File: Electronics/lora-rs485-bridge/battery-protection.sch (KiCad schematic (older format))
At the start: 3 parts

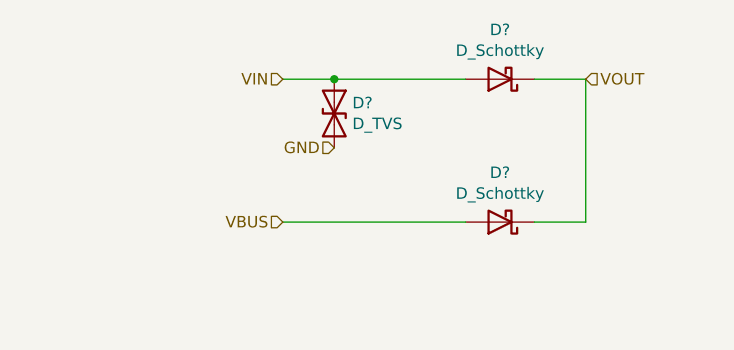
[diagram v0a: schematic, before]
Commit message: Some PCB routing is done
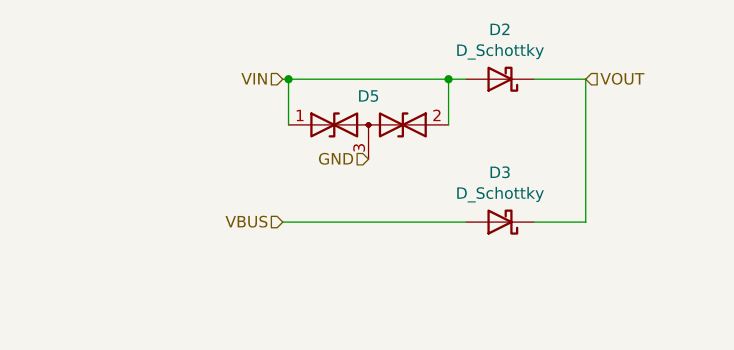
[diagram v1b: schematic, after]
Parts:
- removed D?: D_TVS, symbol Device:D_TVS
- removed D? (x2): D_Schottky, symbol Device:D_Schottky
- added D2, D3: D_Schottky, Diode_SMD:D_SOD-123F, symbol Device:D_Schottky
- added D5: D_TVS_x2_AAC, miceuz-lib:SC89, symbol Device:D_TVS_x2_AAC
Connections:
- net GND: now also D5.3 (common)
- net VBUS: now also D3.2 (A)
- net VIN: now also D2.2 (A), D5.1 (A1), D5.2 (A2)
- net VOUT: now also D2.1 (K), D3.1 (K)
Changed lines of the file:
@@
 EESchema Schematic File Version 5
-LIBS:lora-bridge-cache
 EELAYER 30 0
 EELAYER END
 $Descr A4 11693 8268
 encoding utf-8
-Sheet 2 5
+Sheet 5 5
 Title ""
 Date ""
@@
 	3500 1800 3725 1800
 $Comp
-L Device:D_Schottky D?
+L Device:D_Schottky D2
 U 1 1 5D8754F6
 P 3350 1800
-F 0 "D?" H 3350 1584 50  0000 C CNN
+F 0 "D2" H 3350 1584 50  0000 C CNN
 F 1 "D_Schottky" H 3350 1675 50  0000 C CNN
-F 2 "" H 3350 1800 50  0001 C CNN
+F 2 "Diode_SMD:D_SOD-123F" H 3350 1800 50  0001 C CNN
 F 3 "~" H 3350 1800 50  0001 C CNN
+F 4 "ON SEMICONDUCTOR" H 3350 1800 50  0001 C CNN "Manufacturer"
+F 5 "MBR1020VL" H 3350 1800 50  0001 C CNN "PartNo"
 	1    3350 1800
 	-1   0    0    1
 $EndComp
 $Comp
-L Device:D_TVS D?
-U 1 1 5D877A3B
-P 2625 1950
-F 0 "D?" V 2579 2029 50  0000 L CNN
-F 1 "D_TVS" V 2670 2029 50  0000 L CNN
-F 2 "" H 2625 1950 50  0001 C CNN
-F 3 "~" H 2625 1950 50  0001 C CNN
-	1    2625 1950
-	0    1    1    0
-$EndComp
-Wire Wire Line
-	2400 1800 2625 1800
-Connection ~ 2625 1800
-Wire Wire Line
-	2625 1800 3200 1800
-$Comp
-L Device:D_Schottky D?
-U 1 1 5D8754F6
+L Device:D_Schottky D3
+U 1 1 5D86D14C
 P 3350 2425
-F 0 "D?" H 3350 2209 50  0000 C CNN
+F 0 "D3" H 3350 2209 50  0000 C CNN
 F 1 "D_Schottky" H 3350 2300 50  0000 C CNN
-F 2 "" H 3350 2425 50  0001 C CNN
+F 2 "Diode_SMD:D_SOD-123F" H 3350 2425 50  0001 C CNN
 F 3 "~" H 3350 2425 50  0001 C CNN
+F 4 "ON SEMICONDUCTOR" H 3350 2425 50  0001 C CNN "Manufacturer"
+F 5 "MBR1020VL" H 3350 2425 50  0001 C CNN "PartNo"
 	1    3350 2425
 	-1   0    0    1
@@
 Wire Wire Line
 	2400 2425 3200 2425
-Text HLabel 2625 2100 0    50   Input ~ 0
+Text HLabel 2775 2150 0    50   Input ~ 0
 GND
+$Comp
+L Device:D_TVS_x2_AAC D5
+U 1 1 5D880D1E
+P 2775 2000
+F 0 "D5" H 2775 2125 50  0000 C CNN
+F 1 "D_TVS_x2_AAC" H 2775 2125 50  0001 C CNN
+F 2 "miceuz-lib:SC89" H 2625 2000 50  0001 C CNN
+F 3 "~" H 2625 2000 50  0001 C CNN
+F 4 "ON SEMICONDUCTOR" H 725 300 50  0001 C CNN "Manufacturer"
+F 5 " NZL5V6AXV3T1G" H 725 300 50  0001 C CNN "PartNo"
+	1    2775 2000
+	1    0    0    -1
+$EndComp
+Wire Wire Line
+	2400 1800 2425 1800
+Wire Wire Line
+	2425 2000 2425 1800
+Connection ~ 2425 1800
+Wire Wire Line
+	2425 1800 3125 1800
+Wire Wire Line
+	3125 2000 3125 1800
+Connection ~ 3125 1800
+Wire Wire Line
+	3125 1800 3200 1800
 $EndSCHEMATC

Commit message: Add ESD protection to i2c lines, change VIN TVS diode to higher voltage, add series resistors to SPI lines, compress the PCB to be at width of typical 4xAA battery holder
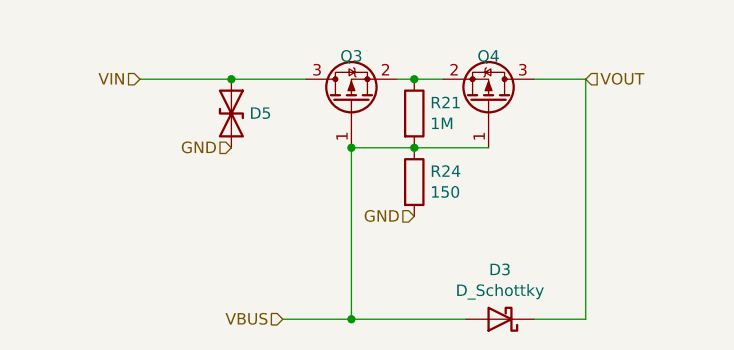
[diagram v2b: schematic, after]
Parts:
- removed D2: D_Schottky, Diode_SMD:D_SOD-123F, symbol Device:D_Schottky
- removed D5: D_TVS_x2_AAC, miceuz-lib:SC89, symbol Device:D_TVS_x2_AAC
- added D5: D_TVS, Diode_SMD:D_SOD-123F, symbol Device:D_TVS
- added Q3, Q4: Q_PMOS_GSD, Package_TO_SOT_SMD:SOT-23, symbol Device:Q_PMOS_GSD
- added R21: 1M, Resistor_SMD:R_0603_1608Metric, symbol Device:R
- added R24: 150, Resistor_SMD:R_0603_1608Metric, symbol Device:R
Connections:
- net GND: now also D5.2 (A2), R24.2
- net VBUS: now also Q3.1 (G), Q4.1 (G), R21.2, R24.1
- net VIN: now also D5.1 (A1), Q3.3 (D)
- net VOUT: now also Q4.3 (D)
- new net: Q3.2 (S), Q4.2 (S), R21.1
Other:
- moved on the sheet: D3
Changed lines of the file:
@@
 $Descr A4 11693 8268
 encoding utf-8
-Sheet 5 5
+Sheet 4 5
 Title ""
 Date ""
@@
 Comment9 ""
 $EndDescr
-Text HLabel 2400 1800 0    50   Input ~ 0
+Text HLabel 1775 1800 0    50   Input ~ 0
 VIN
 Text HLabel 3725 1800 2    50   Input ~ 0
 VOUT
-Text HLabel 2400 2425 0    50   Input ~ 0
+Text HLabel 2400 2850 0    50   Input ~ 0
 VBUS
 Wire Wire Line
 	3500 1800 3725 1800
 $Comp
-L Device:D_Schottky D2
-U 1 1 5D8754F6
-P 3350 1800
-F 0 "D2" H 3350 1584 50  0000 C CNN
-F 1 "D_Schottky" H 3350 1675 50  0000 C CNN
-F 2 "Diode_SMD:D_SOD-123F" H 3350 1800 50  0001 C CNN
-F 3 "~" H 3350 1800 50  0001 C CNN
-F 4 "ON SEMICONDUCTOR" H 3350 1800 50  0001 C CNN "Manufacturer"
-F 5 "MBR1020VL" H 3350 1800 50  0001 C CNN "PartNo"
-	1    3350 1800
-	-1   0    0    1
-$EndComp
-$Comp
 L Device:D_Schottky D3
 U 1 1 5D86D14C
-P 3350 2425
-F 0 "D3" H 3350 2209 50  0000 C CNN
-F 1 "D_Schottky" H 3350 2300 50  0000 C CNN
-F 2 "Diode_SMD:D_SOD-123F" H 3350 2425 50  0001 C CNN
-F 3 "~" H 3350 2425 50  0001 C CNN
-F 4 "ON SEMICONDUCTOR" H 3350 2425 50  0001 C CNN "Manufacturer"
-F 5 "MBR1020VL" H 3350 2425 50  0001 C CNN "PartNo"
-	1    3350 2425
+P 3350 2850
+F 0 "D3" H 3350 2634 50  0000 C CNN
+F 1 "D_Schottky" H 3350 2725 50  0000 C CNN
+F 2 "Diode_SMD:D_SOD-123F" H 3350 2850 50  0001 C CNN
+F 3 "~" H 3350 2850 50  0001 C CNN
+F 4 "ON SEMICONDUCTOR" H 3350 2850 50  0001 C CNN "Manufacturer"
+F 5 "MBR1020VL" H 3350 2850 50  0001 C CNN "PartNo"
+	1    3350 2850
 	-1   0    0    1
 $EndComp
 Wire Wire Line
-	3725 1800 3725 2425
+	3725 1800 3725 2850
 Wire Wire Line
-	3500 2425 3725 2425
+	3500 2850 3725 2850
 Wire Wire Line
-	2400 2425 3200 2425
-Text HLabel 2775 2150 0    50   Input ~ 0
+	2400 2850 2700 2850
+Text HLabel 2175 2100 0    50   Input ~ 0
 GND
 $Comp
-L Device:D_TVS_x2_AAC D5
-U 1 1 5D880D1E
-P 2775 2000
-F 0 "D5" H 2775 2125 50  0000 C CNN
-F 1 "D_TVS_x2_AAC" H 2775 2125 50  0001 C CNN
-F 2 "miceuz-lib:SC89" H 2625 2000 50  0001 C CNN
-F 3 "~" H 2625 2000 50  0001 C CNN
-F 4 "ON SEMICONDUCTOR" H 725 300 50  0001 C CNN "Manufacturer"
-F 5 " NZL5V6AXV3T1G" H 725 300 50  0001 C CNN "PartNo"
-	1    2775 2000
+L Device:D_TVS D5
+U 1 1 5DC183A7
+P 2175 1950
+F 0 "D5" V 2175 2029 50  0000 L CNN
+F 1 "D_TVS" V 2220 2029 50  0001 L CNN
+F 2 "Diode_SMD:D_SOD-123F" H 2175 1950 50  0001 C CNN
+F 3 "~" H 2175 1950 50  0001 C CNN
+F 4 "SMF11A" H 2175 1950 50  0001 C CNN "PartNo"
+F 5 "Littlefuse" H 2175 1950 50  0001 C CNN "Manufacturer"
+	1    2175 1950
+	0    1    1    0
+$EndComp
+Wire Wire Line
+	1775 1800 2175 1800
+$Comp
+L Device:Q_PMOS_GSD Q3
+U 1 1 5DC1ADD3
+P 2700 1900
+F 0 "Q3" V 2900 1900 50  0000 C CNN
+F 1 "Q_PMOS_GSD" V 2937 1900 50  0001 C CNN
+F 2 "Package_TO_SOT_SMD:SOT-23" H 2900 2000 29  0001 C CNN
+F 3 "" H 2700 1900 60  0000 C CNN
+F 4 "NX2301P,215 " H 2700 1900 60  0001 C CNN "PartNo"
+F 5 "NXP" H 2700 1900 60  0001 C CNN "Manufacturer"
+F 6 "1894738" H 2700 1900 60  0001 C CNN "Distributor"
+F 7 "Exact as specified" H 2700 1900 50  0001 C CNN "Comment"
+	1    2700 1900
+	0    -1   -1   0
+$EndComp
+$Comp
+L Device:Q_PMOS_GSD Q4
+U 1 1 5DC24989
+P 3300 1900
+F 0 "Q4" V 3500 1900 50  0000 C CNN
+F 1 "Q_PMOS_GSD" V 3537 1900 50  0001 C CNN
+F 2 "Package_TO_SOT_SMD:SOT-23" H 3500 2000 29  0001 C CNN
+F 3 "" H 3300 1900 60  0000 C CNN
+F 4 "NX2301P,215 " H 3300 1900 60  0001 C CNN "PartNo"
+F 5 "NXP" H 3300 1900 60  0001 C CNN "Manufacturer"
+F 6 "1894738" H 3300 1900 60  0001 C CNN "Distributor"
+F 7 "Exact as specified" H 3300 1900 50  0001 C CNN "Comment"
+	1    3300 1900
+	0    1    -1   0
+$EndComp
+$Comp
+L Device:R R21
+U 1 1 5DC1D764
+P 2975 1950
+F 0 "R21" H 3045 1996 50  0000 L CNN
+F 1 "1M" H 3045 1905 50  0000 L CNN
+F 2 "Resistor_SMD:R_0603_1608Metric" V 2905 1950 50  0001 C CNN
+F 3 "~" H 2975 1950 50  0001 C CNN
+	1    2975 1950
 	1    0    0    -1
 $EndComp
 Wire Wire Line
-	2400 1800 2425 1800
+	2900 1800 2975 1800
+Connection ~ 2975 1800
 Wire Wire Line
-	2425 2000 2425 1800
-Connection ~ 2425 1800
+	2975 1800 3100 1800
 Wire Wire Line
-	2425 1800 3125 1800
+	2700 2100 2975 2100
+Connection ~ 2975 2100
 Wire Wire Line
-	3125 2000 3125 1800
-Connection ~ 3125 1800
+	2975 2100 3300 2100
 Wire Wire Line
-	3125 1800 3200 1800
+	2175 1800 2500 1800
+Connection ~ 2175 1800
+$Comp
+L Device:R R24
+U 1 1 5DC22CF0
+P 2975 2250
+F 0 "R24" H 3045 2296 50  0000 L CNN
+F 1 "150" H 3045 2205 50  0000 L CNN
+F 2 "Resistor_SMD:R_0603_1608Metric" V 2905 2250 50  0001 C CNN
+F 3 "~" H 2975 2250 50  0001 C CNN
+	1    2975 2250
+	1    0    0    -1
+$EndComp
+Text HLabel 2975 2400 0    50   Input ~ 0
+GND
+Wire Wire Line
+	2700 2100 2700 2850
+Connection ~ 2700 2100
+Connection ~ 2700 2850
+Wire Wire Line
+	2700 2850 3200 2850
 $EndSCHEMATC

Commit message: Add power input PTC fuse
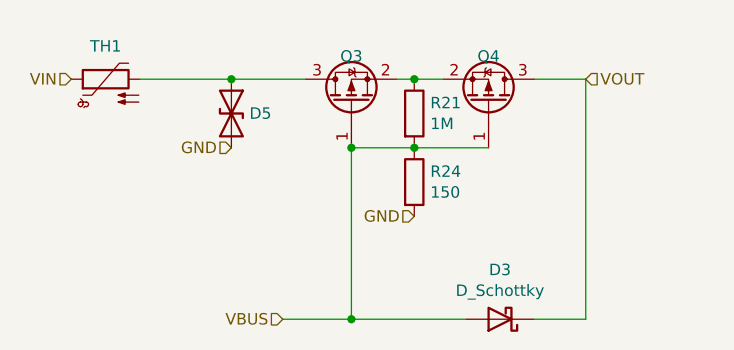
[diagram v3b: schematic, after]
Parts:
- added TH1: Thermistor_PTC, Fuse:Fuse_1206_3216Metric, symbol Device:Thermistor_PTC
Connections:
- net VIN: now also TH1.1; no longer D5.1 (A1), Q3.3 (D)
- new net: D5.1 (A1), Q3.3 (D), TH1.2
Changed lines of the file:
@@
 Comment9 ""
 $EndDescr
-Text HLabel 1775 1800 0    50   Input ~ 0
+Text HLabel 1475 1800 0    50   Input ~ 0
 VIN
 Text HLabel 3725 1800 2    50   Input ~ 0
@@
 Wire Wire Line
 	2700 2850 3200 2850
+$Comp
+L Device:Thermistor_PTC TH1
+U 1 1 5DC19068
+P 1625 1800
+F 0 "TH1" V 1769 1800 50  0000 C CNN
+F 1 "Thermistor_PTC" V 1769 1800 50  0001 C CNN
+F 2 "Fuse:Fuse_1206_3216Metric" H 1675 1600 50  0001 L CNN
+F 3 "~" H 1625 1800 50  0001 C CNN
+F 4 "nSMD075-13.2V" H 1625 1800 50  0001 C CNN "PartNo"
+F 5 "TECHFUSE" H 1625 1800 50  0001 C CNN "Manufacturer"
+	1    1625 1800
+	0    -1   -1   0
+$EndComp
 $EndSCHEMATC

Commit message: Update D3 to silicone diode as schottky leaks as hell; Add D2 to protect gates of mosfets; Remove series resistors from RFM95 interface, add pullups/downs for better sleep stability; Unify resistor values across the board; Bump version number to v1.2
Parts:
- added D2: 7.6V, Diode_SMD:D_SOD-323, symbol Device:D_Zener
- D3: value D_Schottky -> 1N4148; footprint Diode_SMD:D_SOD-123F -> Diode_SMD:D_SOD-123; symbol Device:D_Schottky -> Device:D; Manufacturer ON SEMICONDUCTOR -> Diodes Inc; PartNo MBR1020VL -> 1N4148W-7-F
- R24: value 150 -> 1M
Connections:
- net VBUS: now also D2.2 (A)
- net at Q3.2 (S), Q4.2 (S), R21.1: now also D2.1 (K)
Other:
- moved on the sheet: D3, Q4, R21, R24
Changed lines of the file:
@@
 $Descr A4 11693 8268
 encoding utf-8
-Sheet 4 5
+Sheet 2 5
 Title ""
 Date ""
@@
 	0    -1   -1   0
 $EndComp
-Text HLabel 3725 1800 2    50   Input ~ 0
-VOUT
-$Comp
-L Device:D_Schottky D3
-U 1 1 5D86D14C
-P 3350 2850
-F 0 "D3" H 3350 2634 50  0000 C CNN
-F 1 "D_Schottky" H 3350 2725 50  0000 C CNN
-F 2 "Diode_SMD:D_SOD-123F" H 3350 2850 50  0001 C CNN
-F 3 "~" H 3350 2850 50  0001 C CNN
-F 4 "ON SEMICONDUCTOR" H 3350 2850 50  0001 C CNN "Manufacturer"
-F 5 "MBR1020VL" H 3350 2850 50  0001 C CNN "PartNo"
-	1    3350 2850
-	-1   0    0    1
-$EndComp
 Wire Wire Line
-	3725 1800 3725 2850
-Wire Wire Line
-	3500 2850 3725 2850
-Wire Wire Line
-	3500 1800 3725 1800
+	3775 1800 4000 1800
 $Comp
 L Device:Q_PMOS_GSD Q4
 U 1 1 5DC24989
-P 3300 1900
-F 0 "Q4" V 3500 1900 50  0000 C CNN
-F 1 "Q_PMOS_GSD" V 3537 1900 50  0001 C CNN
-F 2 "Package_TO_SOT_SMD:SOT-23" H 3500 2000 29  0001 C CNN
-F 3 "" H 3300 1900 60  0000 C CNN
-F 4 "NX2301P,215 " H 3300 1900 60  0001 C CNN "PartNo"
-F 5 "NXP" H 3300 1900 60  0001 C CNN "Manufacturer"
-F 6 "1894738" H 3300 1900 60  0001 C CNN "Distributor"
-F 7 "Exact as specified" H 3300 1900 50  0001 C CNN "Comment"
-	1    3300 1900
+P 3575 1900
+F 0 "Q4" V 3775 1900 50  0000 C CNN
+F 1 "Q_PMOS_GSD" V 3812 1900 50  0001 C CNN
+F 2 "Package_TO_SOT_SMD:SOT-23" H 3775 2000 29  0001 C CNN
+F 3 "" H 3575 1900 60  0000 C CNN
+F 4 "NX2301P,215 " H 3575 1900 60  0001 C CNN "PartNo"
+F 5 "NXP" H 3575 1900 60  0001 C CNN "Manufacturer"
+F 6 "1894738" H 3575 1900 60  0001 C CNN "Distributor"
+F 7 "Exact as specified" H 3575 1900 50  0001 C CNN "Comment"
+	1    3575 1900
 	0    1    -1   0
 $EndComp
+Connection ~ 3250 1800
 Wire Wire Line
-	2975 1800 3100 1800
-Wire Wire Line
-	2975 2100 3300 2100
-$Comp
-L Device:R R21
-U 1 1 5DC1D764
-P 2975 1950
-F 0 "R21" H 3045 1996 50  0000 L CNN
-F 1 "1M" H 3045 1905 50  0000 L CNN
-F 2 "Resistor_SMD:R_0603_1608Metric" V 2905 1950 50  0001 C CNN
-F 3 "~" H 2975 1950 50  0001 C CNN
-	1    2975 1950
-	1    0    0    -1
-$EndComp
-Wire Wire Line
-	2900 1800 2975 1800
-Connection ~ 2975 1800
-Wire Wire Line
-	2700 2100 2975 2100
-Connection ~ 2975 2100
-Text HLabel 2975 2400 0    50   Input ~ 0
-GND
-Text HLabel 2400 2850 0    50   Input ~ 0
-VBUS
-Wire Wire Line
-	2400 2850 2700 2850
-$Comp
-L Device:R R24
-U 1 1 5DC22CF0
-P 2975 2250
-F 0 "R24" H 3045 2296 50  0000 L CNN
-F 1 "150" H 3045 2205 50  0000 L CNN
-F 2 "Resistor_SMD:R_0603_1608Metric" V 2905 2250 50  0001 C CNN
-F 3 "~" H 2975 2250 50  0001 C CNN
-	1    2975 2250
-	1    0    0    -1
-$EndComp
-Wire Wire Line
-	2700 2100 2700 2850
-Connection ~ 2700 2850
-Wire Wire Line
-	2700 2850 3200 2850
-$Comp
-L Device:D_TVS D5
-U 1 1 5DC183A7
-P 2175 1950
-F 0 "D5" V 2175 2029 50  0000 L CNN
-F 1 "D_TVS" V 2220 2029 50  0001 L CNN
-F 2 "Diode_SMD:D_SOD-123F" H 2175 1950 50  0001 C CNN
-F 3 "~" H 2175 1950 50  0001 C CNN
-F 4 "SMF11A" H 2175 1950 50  0001 C CNN "PartNo"
-F 5 "Littlefuse" H 2175 1950 50  0001 C CNN "Manufacturer"
-	1    2175 1950
-	0    1    1    0
-$EndComp
+	3250 1800 3375 1800
+Text HLabel 4000 1800 2    50   Input ~ 0
+VOUT
 $Comp
 L Device:Q_PMOS_GSD Q3
@@
 Wire Wire Line
 	2175 1800 2500 1800
+$Comp
+L Device:D_TVS D5
+U 1 1 5DC183A7
+P 2175 1950
+F 0 "D5" V 2175 2029 50  0000 L CNN
+F 1 "D_TVS" V 2220 2029 50  0001 L CNN
+F 2 "Diode_SMD:D_SOD-123F" H 2175 1950 50  0001 C CNN
+F 3 "~" H 2175 1950 50  0001 C CNN
+F 4 "SMF11A" H 2175 1950 50  0001 C CNN "PartNo"
+F 5 "Littlefuse" H 2175 1950 50  0001 C CNN "Manufacturer"
+	1    2175 1950
+	0    1    1    0
+$EndComp
+Connection ~ 2950 1800
+Connection ~ 2950 2100
+Wire Wire Line
+	2700 2100 2700 2850
+Text HLabel 2400 2850 0    50   Input ~ 0
+VBUS
+Connection ~ 2700 2850
+Wire Wire Line
+	2400 2850 2700 2850
 Connection ~ 2700 2100
+Wire Wire Line
+	2700 2850 3475 2850
+Text HLabel 3250 2400 0    50   Input ~ 0
+GND
+Wire Wire Line
+	2950 2100 3250 2100
+Connection ~ 3250 2100
+Wire Wire Line
+	3250 2100 3575 2100
+Wire Wire Line
+	4000 1800 4000 2850
+$Comp
+L Device:R R24
+U 1 1 5DC22CF0
+P 3250 2250
+F 0 "R24" H 3320 2296 50  0000 L CNN
+F 1 "1M" H 3320 2205 50  0000 L CNN
+F 2 "Resistor_SMD:R_0603_1608Metric" V 3180 2250 50  0001 C CNN
+F 3 "~" H 3250 2250 50  0001 C CNN
+	1    3250 2250
+	1    0    0    -1
+$EndComp
+$Comp
+L Device:D D3
+U 1 1 5D86D14C
+P 3625 2850
+F 0 "D3" H 3625 2634 50  0000 C CNN
+F 1 "1N4148" H 3625 2725 50  0000 C CNN
+F 2 "Diode_SMD:D_SOD-123" H 3625 2850 50  0001 C CNN
+F 3 "~" H 3625 2850 50  0001 C CNN
+F 4 "Diodes Inc" H 3625 2850 50  0001 C CNN "Manufacturer"
+F 5 "1N4148W-7-F" H 3625 2850 50  0001 C CNN "PartNo"
+	1    3625 2850
+	-1   0    0    1
+$EndComp
+Wire Wire Line
+	3775 2850 4000 2850
+Wire Wire Line
+	2700 2100 2950 2100
+$Comp
+L Device:R R21
+U 1 1 5DC1D764
+P 3250 1950
+F 0 "R21" H 3320 1996 50  0000 L CNN
+F 1 "1M" H 3320 1905 50  0000 L CNN
+F 2 "Resistor_SMD:R_0603_1608Metric" V 3180 1950 50  0001 C CNN
+F 3 "~" H 3250 1950 50  0001 C CNN
+	1    3250 1950
+	1    0    0    -1
+$EndComp
+$Comp
+L Device:D_Zener D2
+U 1 1 5E21FE6A
+P 2950 1950
+F 0 "D2" V 2905 2030 50  0000 L CNN
+F 1 "7.6V" V 2995 2030 50  0000 L CNN
+F 2 "Diode_SMD:D_SOD-323" H 2950 1950 50  0001 C CNN
+F 3 "~" H 2950 1950 50  0001 C CNN
+F 4 "MM3Z7V5ST1G" H 2950 1950 50  0001 C CNN "PartNo"
+F 5 "ON SEMI" H 2950 1950 50  0001 C CNN "Manufacturer"
+	1    2950 1950
+	0    1    1    0
+$EndComp
+Wire Wire Line
+	2900 1800 2950 1800
+Wire Wire Line
+	2950 1800 3250 1800
 $EndSCHEMATC
